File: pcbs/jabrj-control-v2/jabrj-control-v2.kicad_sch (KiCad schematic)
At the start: 8 parts

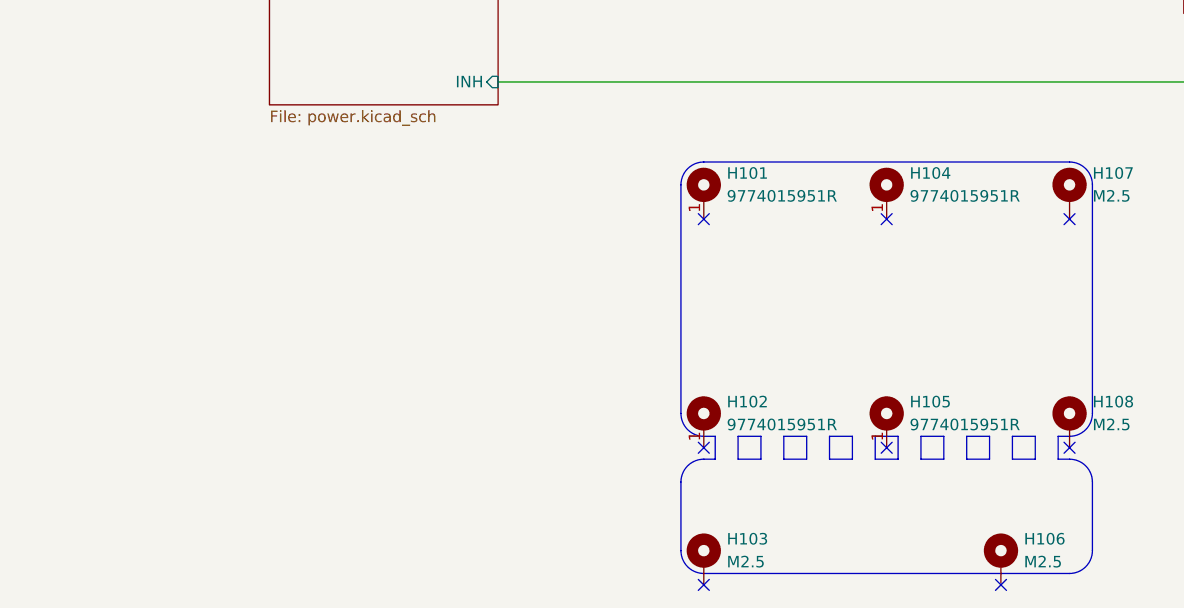
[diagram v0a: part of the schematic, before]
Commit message: Fixed 5V buck inductor value
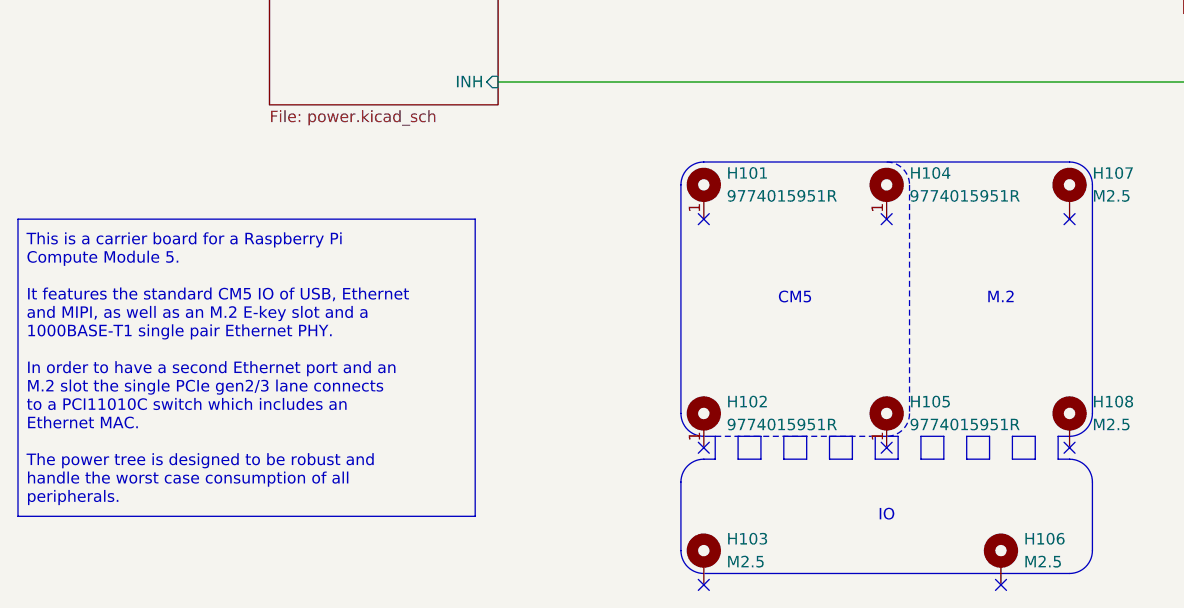
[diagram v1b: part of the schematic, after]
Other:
- note added: "CM5"
- note added: "IO"
- note added: "M.2"
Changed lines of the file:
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@@
 	)
 	(arc
+		(start 134.62 173.99)
+		(mid 133.8761 175.7861)
+		(end 132.08 176.53)
+		(stroke
+			(width 0)
+			(type dash)
+		)
+		(fill
+			(type none)
+		)
+	)
+	(arc
+		(start 132.08 146.05)
+		(mid 133.8761 146.7939)
+		(end 134.62 148.59)
+		(stroke
+			(width 0)
+			(type dash)
+		)
+		(fill
+			(type none)
+		)
+	)
+	(arc
 		(start 109.22 181.61)
 		(mid 109.9639 179.8139)
@@
 		)
 	)
+	(text "IO"
+		(exclude_from_sim no)
+		(at 132.08 185.42 0)
+		(effects
+			(font
+				(size 1.27 1.27)
+			)
+		)
+	)
 	(text "Can be broken off\nif IO isn't needed"
 		(exclude_from_sim no)
@@
 		)
 	)
+	(text "CM5"
+		(exclude_from_sim no)
+		(at 121.92 161.29 0)
+		(effects
+			(font
+				(size 1.27 1.27)
+			)
+		)
+	)
+	(text "M.2"
+		(exclude_from_sim no)
+		(at 144.78 161.29 0)
+		(effects
+			(font
+				(size 1.27 1.27)
+			)
+		)
+	)
+	(text_box "This is a carrier board for a Raspberry Pi Compute Module 5.\n\nIt features the standard CM5 IO of USB, Ethernet and MIPI, as well as an M.2 E-key slot and a 1000BASE-T1 single pair Ethernet PHY.\n\nIn order to have a second Ethernet port and an M.2 slot the single PCIe gen2/3 lane connects to a PCI11010C switch which includes an Ethernet MAC.\n\nThe power tree is designed to be robust and handle the worst case consumption of all peripherals."
+		(exclude_from_sim no)
+		(at 35.56 152.4 0)
+		(size 50.8 33.02)
+		(margins 0.9525 0.9525 0.9525 0.9525)
+		(stroke
+			(width 0)
+			(type solid)
+		)
+		(fill
+			(type none)
+		)
+		(effects
+			(font
+				(size 1.27 1.27)
+			)
+			(justify left)
+		)
+	)
 	(junction
 		(at 152.4 55.88)
@@
 		)
 	)
+	(polyline
+		(pts
+			(xy 113.03 176.53) (xy 130.81 176.53)
+		)
+		(stroke
+			(width 0)
+			(type dash)
+		)
+	)
 	(wire
 		(pts
@@
 		)
 	)
+	(polyline
+		(pts
+			(xy 134.62 148.59) (xy 134.62 173.99)
+		)
+		(stroke
+			(width 0)
+			(type dash)
+		)
+	)
 	(bus
 		(pts
@@
 		)
 		(instances
-			(project "jabr-control-v2"
+			(project "jabrj-control-v2"
 				(path "/f91ec272-d09a-4038-bbbb-962739a92c51"
 					(reference "H105")
@@
 		)
 		(instances
-			(project "jabr-control-v2"
+			(project "jabrj-control-v2"
 				(path "/f91ec272-d09a-4038-bbbb-962739a92c51"
 					(reference "H107")
@@
 		)
 		(instances
-			(project "jabr-control-v2"
+			(project "jabrj-control-v2"
 				(path "/f91ec272-d09a-4038-bbbb-962739a92c51"
 					(reference "H102")
@@
 		)
 		(instances
-			(project "jabr-control-v2"
+			(project "jabrj-control-v2"
 				(path "/f91ec272-d09a-4038-bbbb-962739a92c51"
 					(reference "H101")
@@
 		)
 		(instances
-			(project "jabr-control-v2"
+			(project "jabrj-control-v2"
 				(path "/f91ec272-d09a-4038-bbbb-962739a92c51"
 					(reference "H106")
@@
 		)
 		(instances
-			(project "jabr-control-v2"
+			(project "jabrj-control-v2"
 				(path "/f91ec272-d09a-4038-bbbb-962739a92c51"
 					(reference "H104")
@@
 		)
 		(instances
-			(project "jabr-control-v2"
+			(project "jabrj-control-v2"
 				(path "/f91ec272-d09a-4038-bbbb-962739a92c51"
 					(reference "H103")
@@
 		)
 		(instances
-			(project "jabr-control-v2"
+			(project "jabrj-control-v2"
 				(path "/f91ec272-d09a-4038-bbbb-962739a92c51"
 					(reference "H108")
@@
 		)
 		(instances
-			(project "jabr-control-v2"
+			(project "jabrj-control-v2"
 				(path "/f91ec272-d09a-4038-bbbb-962739a92c51"
 					(page "12")
@@
 		)
 		(instances
-			(project "jabr-control-v2"
+			(project "jabrj-control-v2"
 				(path "/f91ec272-d09a-4038-bbbb-962739a92c51"
 					(page "2")
@@
 		)
 		(instances
-			(project "jabr-control-v2"
+			(project "jabrj-control-v2"
 				(path "/f91ec272-d09a-4038-bbbb-962739a92c51"
 					(page "10")
@@
 		)
 		(instances
-			(project "jabr-control-v2"
+			(project "jabrj-control-v2"
 				(path "/f91ec272-d09a-4038-bbbb-962739a92c51"
 					(page "7")
@@
 		)
 		(instances
-			(project "jabr-control-v2"
+			(project "jabrj-control-v2"
 				(path "/f91ec272-d09a-4038-bbbb-962739a92c51"
 					(page "11")
@@
 		)
 		(instances
-			(project "jabr-control-v2"
+			(project "jabrj-control-v2"
 				(path "/f91ec272-d09a-4038-bbbb-962739a92c51"
 					(page "9")
@@
 		)
 		(instances
-			(project "jabr-control-v2"
+			(project "jabrj-control-v2"
 				(path "/f91ec272-d09a-4038-bbbb-962739a92c51"
 					(page "8")

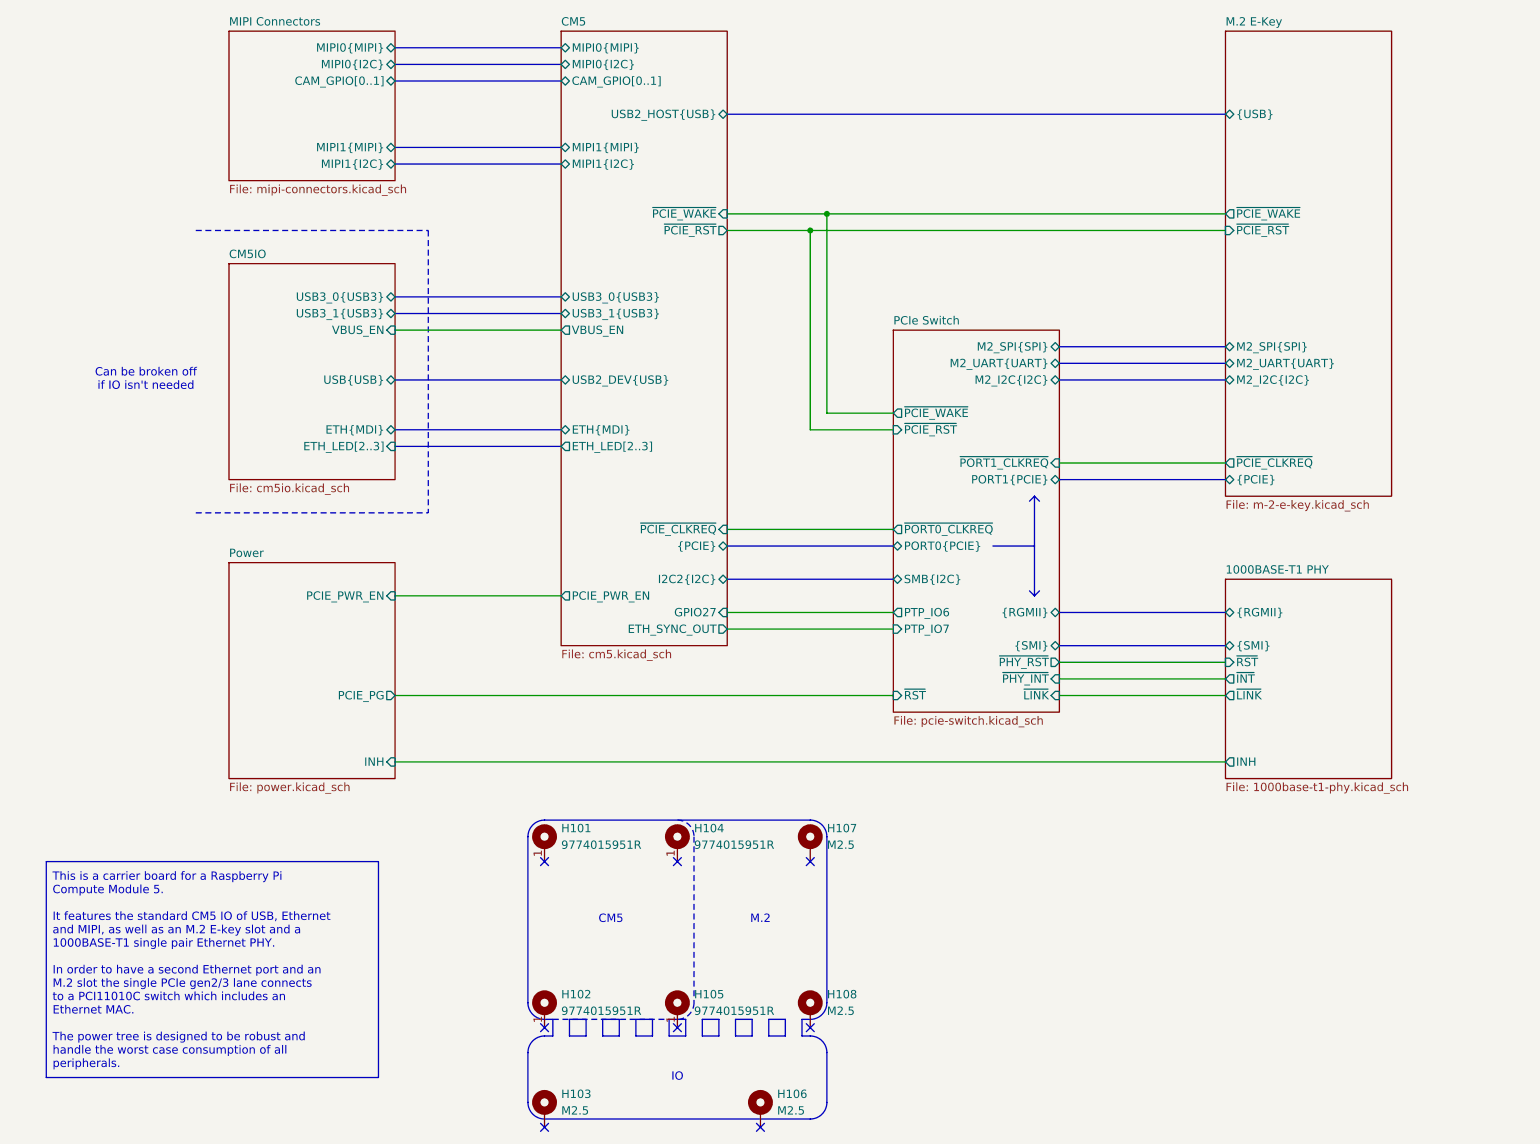
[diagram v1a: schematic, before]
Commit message: Minor schematic fixes
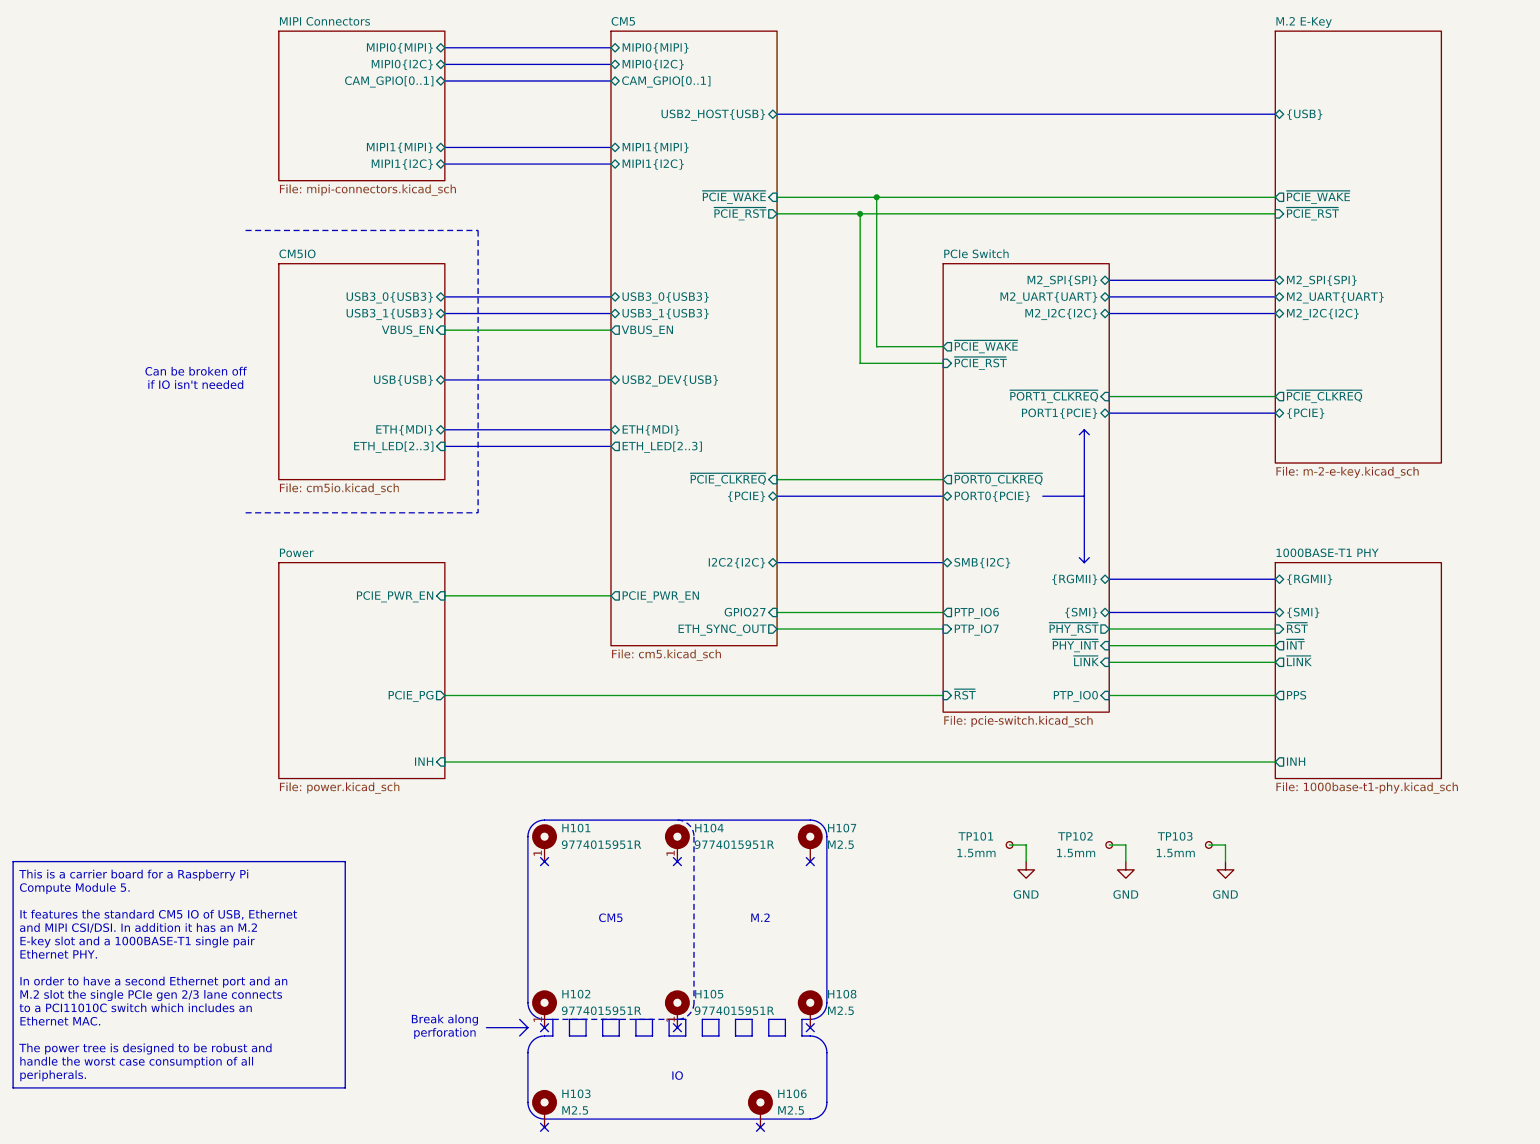
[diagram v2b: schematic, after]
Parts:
- added TP101, TP102, TP103: 1.5mm, project_footprints:TestPoint_Pad_D1.5mm, symbol Connector:TestPoint_Small
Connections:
- new net GND: TP101.1, TP102.1, TP103.1
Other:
- sheet 1000BASE-T1 PHY ports: added PPS; removed none
- sheet PCIe Switch ports: added PTP_IO0; removed none
- note added: "Break along perforation"

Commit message: Layout started
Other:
- moved on the sheet: H106
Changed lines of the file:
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@@
 	)
 	(no_connect
-		(at 144.78 193.04)
+		(at 152.4 193.04)
 	)
 	(bus
@@
 	(symbol
 		(lib_id "Mechanical:MountingHole_Pad")
-		(at 144.78 190.5 0)
+		(at 152.4 190.5 0)
 		(unit 1)
 		(body_style 1)
@@
 		(fields_autoplaced yes)
 		(property "Reference" "H106"
-			(at 147.32 187.9599 0)
+			(at 154.94 187.9599 0)
 			(show_name no)
 			(do_not_autoplace no)
@@
 		)
 		(property "Value" "M2.5"
-			(at 147.32 190.4999 0)
+			(at 154.94 190.4999 0)
 			(show_name no)
 			(do_not_autoplace no)
@@
 		)
 		(property "Footprint" "MountingHole:MountingHole_2.7mm_M2.5_Pad"
-			(at 144.78 190.5 0)
+			(at 152.4 190.5 0)
 			(hide yes)
 			(show_name no)
@@
 		)
 		(property "Datasheet" ""
-			(at 144.78 190.5 0)
+			(at 152.4 190.5 0)
 			(hide yes)
 			(show_name no)
@@
 		)
 		(property "Description" "Mounting Hole with connection"
-			(at 144.78 190.5 0)
+			(at 152.4 190.5 0)
 			(hide yes)
 			(show_name no)
@@
 		)
 		(property "Field6" ""
-			(at 144.78 190.5 0)
+			(at 152.4 190.5 0)
 			(hide yes)
 			(show_name no)
@@
 		)
 		(property "Field7" ""
-			(at 144.78 190.5 0)
+			(at 152.4 190.5 0)
 			(hide yes)
 			(show_name no)
@@
 		)
 		(property "Part Description" ""
-			(at 144.78 190.5 0)
+			(at 152.4 190.5 0)
 			(hide yes)
 			(show_name no)
@@
 		)
 		(property "Critical Parameter" ""
-			(at 144.78 190.5 0)
+			(at 152.4 190.5 0)
 			(hide yes)
 			(show_name no)
@@
 		)
 		(property "IRP,40K (A)" ""
-			(at 144.78 190.5 0)
+			(at 152.4 190.5 0)
 			(hide yes)
 			(show_name no)
@@
 		)
 		(property "ISAT,10% (A)" ""
-			(at 144.78 190.5 0)
+			(at 152.4 190.5 0)
 			(hide yes)
 			(show_name no)
@@
 		)
 		(property "ISAT,30% (A)" ""
-			(at 144.78 190.5 0)
+			(at 152.4 190.5 0)
 			(hide yes)
 			(show_name no)
@@
 		)
 		(property "L (µH)" ""
-			(at 144.78 190.5 0)
+			(at 152.4 190.5 0)
 			(hide yes)
 			(show_name no)
@@
 		)
 		(property "Manufacturer" ""
-			(at 144.78 190.5 0)
+			(at 152.4 190.5 0)
 			(hide yes)
 			(show_name no)
@@
 		)
 		(property "Manufacturer URL" ""
-			(at 144.78 190.5 0)
+			(at 152.4 190.5 0)
 			(hide yes)
 			(show_name no)
@@
 		)
 		(property "Match Code" ""
-			(at 144.78 190.5 0)
+			(at 152.4 190.5 0)
 			(hide yes)
 			(show_name no)
@@
 		)
 		(property "Mounting Technology" ""
-			(at 144.78 190.5 0)
+			(at 152.4 190.5 0)
 			(hide yes)
 			(show_name no)
@@
 		)
 		(property "Part Number" ""
-			(at 144.78 190.5 0)
+			(at 152.4 190.5 0)
 			(hide yes)
 			(show_name no)
@@
 		)
 		(property "Published Date" ""
-			(at 144.78 190.5 0)
+			(at 152.4 190.5 0)
 			(hide yes)
 			(show_name no)
@@
 		)
 		(property "RDC max. (mΩ)" ""
-			(at 144.78 190.5 0)
+			(at 152.4 190.5 0)
 			(hide yes)
 			(show_name no)
@@
 		)
 		(property "RDC typ. (mΩ)" ""
-			(at 144.78 190.5 0)
+			(at 152.4 190.5 0)
 			(hide yes)
 			(show_name no)
@@
 		)
 		(property "Size" ""
-			(at 144.78 190.5 0)
+			(at 152.4 190.5 0)
 			(hide yes)
 			(show_name no)
@@
 		)
 		(property "Type/Size" ""
-			(at 144.78 190.5 0)
+			(at 152.4 190.5 0)
 			(hide yes)
 			(show_name no)
@@
 		)
 		(property "VOP (V)" ""
-			(at 144.78 190.5 0)
+			(at 152.4 190.5 0)
 			(hide yes)
 			(show_name no)
@@
 		)
 		(property "fres (MHz)" ""
-			(at 144.78 190.5 0)
-			(hide yes)
-			(show_name no)
+			(at 152.4 190.5 0)
+			(hide yes)
+			(show_name no)

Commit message: 651 Unrouted
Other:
- sheet MIPI Connectors ports: added CAM_GPIO[0..2]; removed CAM_GPIO[0..1]
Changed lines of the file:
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@@
 	(text "Can be broken off\nif IO isn't needed"
 		(exclude_from_sim no)
-		(at 58.42 78.74 0)
+		(at 58.42 81.28 0)
 		(effects
 			(font
@@
 	(bus
 		(pts
-			(xy 96.52 43.18) (xy 121.92 43.18)
+			(xy 96.52 45.72) (xy 121.92 45.72)
 		)
 		(stroke
@@
 	(bus
 		(pts
-			(xy 147.32 38.1) (xy 223.52 38.1)
+			(xy 147.32 33.02) (xy 223.52 33.02)
 		)
 		(stroke
@@
 	(polyline
 		(pts
-			(xy 66.04 99.06) (xy 101.6 99.06)
+			(xy 66.04 96.52) (xy 101.6 96.52)
 		)
 		(stroke
@@
 	(wire
 		(pts
-			(xy 96.52 111.76) (xy 121.92 111.76)
+			(xy 96.52 109.22) (xy 121.92 109.22)
 		)
 		(stroke
@@
 	(bus
 		(pts
-			(xy 96.52 33.02) (xy 121.92 33.02)
+			(xy 96.52 27.94) (xy 121.92 27.94)
 		)
 		(stroke
@@
 	(bus
 		(pts
-			(xy 96.52 45.72) (xy 121.92 45.72)
+			(xy 96.52 48.26) (xy 121.92 48.26)
 		)
 		(stroke
@@
 	(polyline
 		(pts
-			(xy 66.04 55.88) (xy 101.6 55.88)
+			(xy 66.04 58.42) (xy 101.6 58.42)
 		)
 		(stroke
@@
 	(bus
 		(pts
-			(xy 96.52 30.48) (xy 121.92 30.48)
+			(xy 96.52 40.64) (xy 121.92 40.64)
 		)
 		(stroke
@@
 	(bus
 		(pts
-			(xy 96.52 27.94) (xy 121.92 27.94)
+			(xy 96.52 38.1) (xy 121.92 38.1)
 		)
 		(stroke
@@
 	(bus
 		(pts
-			(xy 147.32 106.68) (xy 172.72 106.68)
+			(xy 147.32 104.14) (xy 172.72 104.14)
 		)
 		(stroke
@@
 	(polyline
 		(pts
-			(xy 101.6 55.88) (xy 101.6 99.06)
+			(xy 101.6 58.42) (xy 101.6 96.52)
 		)
 		(stroke
@@
 		)
 		(pin "{USB}" bidirectional
-			(at 223.52 38.1 180)
+			(at 223.52 33.02 180)
 			(effects
 				(font
@@
 	)
 	(sheet
-		(at 71.12 106.68)
-		(size 25.4 33.02)
+		(at 71.12 104.14)
+		(size 25.4 35.56)
 		(exclude_from_sim no)
 		(in_bom yes)
@@
 		)
 		(property "Sheetname" "Power"
-			(at 71.12 105.9684 0)
+			(at 71.12 103.4284 0)
 			(show_name no)
 			(do_not_autoplace no)
@@
 		)
 		(pin "PCIE_PWR_EN" input
-			(at 96.52 111.76 0)
+			(at 96.52 109.22 0)
 			(effects
 				(font
@@
 		)
 		(pin "SMB{I2C}" bidirectional
-			(at 172.72 106.68 180)
+			(at 172.72 104.14 180)
 			(effects
 				(font
@@
 		)
 		(pin "PCIE_PWR_EN" output
-			(at 121.92 111.76 180)
+			(at 121.92 109.22 180)
 			(effects
 				(font
@@
 		)
 		(pin "I2C2{I2C}" bidirectional
-			(at 147.32 106.68 0)
+			(at 147.32 104.14 0)
 			(effects
 				(font
@@
 		)
 		(pin "USB2_HOST{USB}" bidirectional
-			(at 147.32 38.1 0)
+			(at 147.32 33.02 0)
 			(effects
 				(font
@@
 			)
 		)
-		(pin "CAM_GPIO[0..1]" bidirectional
-			(at 121.92 33.02 180)
-			(effects
-				(font
-					(size 1.27 1.27)
-				)
-				(justify left)
-			)
-		)
 		(pin "MIPI0{MIPI}" bidirectional
-			(at 121.92 27.94 180)
+			(at 121.92 38.1 180)
 			(effects
 				(font
@@
 		)
 		(pin "MIPI1{MIPI}" bidirectional
-			(at 121.92 43.18 180)
+			(at 121.92 45.72 180)
 			(effects
 				(font
@@
 		)
 		(pin "MIPI0{I2C}" bidirectional
-			(at 121.92 30.48 180)
+			(at 121.92 40.64 180)
 			(effects
 				(font
@@
 		)
 		(pin "MIPI1{I2C}" bidirectional
-			(at 121.92 45.72 180)
+			(at 121.92 48.26 180)
 			(effects
 				(font
@@
 			)
 		)
+		(pin "CAM_GPIO[0..1]" bidirectional
+			(at 121.92 27.94 180)
+			(effects
+				(font
+					(size 1.27 1.27)
+				)
+				(justify left)
+			)
+		)
 		(instances
 			(project "jabrj-control-v2"
@@
 	(sheet
 		(at 71.12 25.4)
-		(size 25.4 22.86)
+		(size 25.4 25.4)
 		(exclude_from_sim no)
 		(in_bom yes)
@@
 		)
 		(property "Sheetfile" "mipi-connectors.kicad_sch"
-			(at 71.12 48.8446 0)
+			(at 71.12 51.3846 0)
 			(show_name no)
 			(do_not_autoplace no)
@@
 			)
 		)
-		(pin "CAM_GPIO[0..1]" bidirectional
-			(at 96.52 33.02 0)
+		(pin "MIPI0{MIPI}" bidirectional
+			(at 96.52 38.1 0)
 			(effects
 				(font
@@
 			)
 		)
-		(pin "MIPI0{MIPI}" bidirectional
-			(at 96.52 27.94 0)
+		(pin "MIPI1{MIPI}" bidirectional
+			(at 96.52 45.72 0)
 			(effects
 				(font
@@
 			)
 		)
-		(pin "MIPI1{MIPI}" bidirectional
-			(at 96.52 43.18 0)
+		(pin "MIPI0{I2C}" bidirectional
+			(at 96.52 40.64 0)
 			(effects
 				(font
@@
 			)
 		)
-		(pin "MIPI0{I2C}" bidirectional
-			(at 96.52 30.48 0)
+		(pin "MIPI1{I2C}" bidirectional
+			(at 96.52 48.26 0)
 			(effects
 				(font
@@
 			)
 		)
-		(pin "MIPI1{I2C}" bidirectional
-			(at 96.52 45.72 0)
+		(pin "CAM_GPIO[0..2]" bidirectional
+			(at 96.52 27.94 0)
 			(effects
 				(font
@@
 	)
 	(sheet
-		(at 71.12 60.96)
-		(size 25.4 33.02)
+		(at 71.12 63.5)
+		(size 25.4 27.94)
 		(exclude_from_sim no)
 		(in_bom yes)
@@
 		)
 		(property "Sheetname" "CM5IO"
-			(at 71.12 60.2484 0)
+			(at 71.12 62.7884 0)
 			(show_name no)
 			(do_not_autoplace no)
@@
 		)
 		(property "Sheetfile" "cm5io.kicad_sch"
-			(at 71.12 94.5646 0)
+			(at 71.12 92.0246 0)
 			(show_name no)
 			(do_not_autoplace no)
